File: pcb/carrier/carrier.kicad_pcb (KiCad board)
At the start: 2 copper layers, 152 x 100.2 mm, 42 parts, among them J1 Freeze footswitch, J2 Clear footswitch, J3 In L / Mono, J4 In R (normalled from In L), J5 Out L / Mono, J6 Out R (ring = plug detect), SW1 Single / Multi, SW2 +5 up / down, U1 Daisy Seed

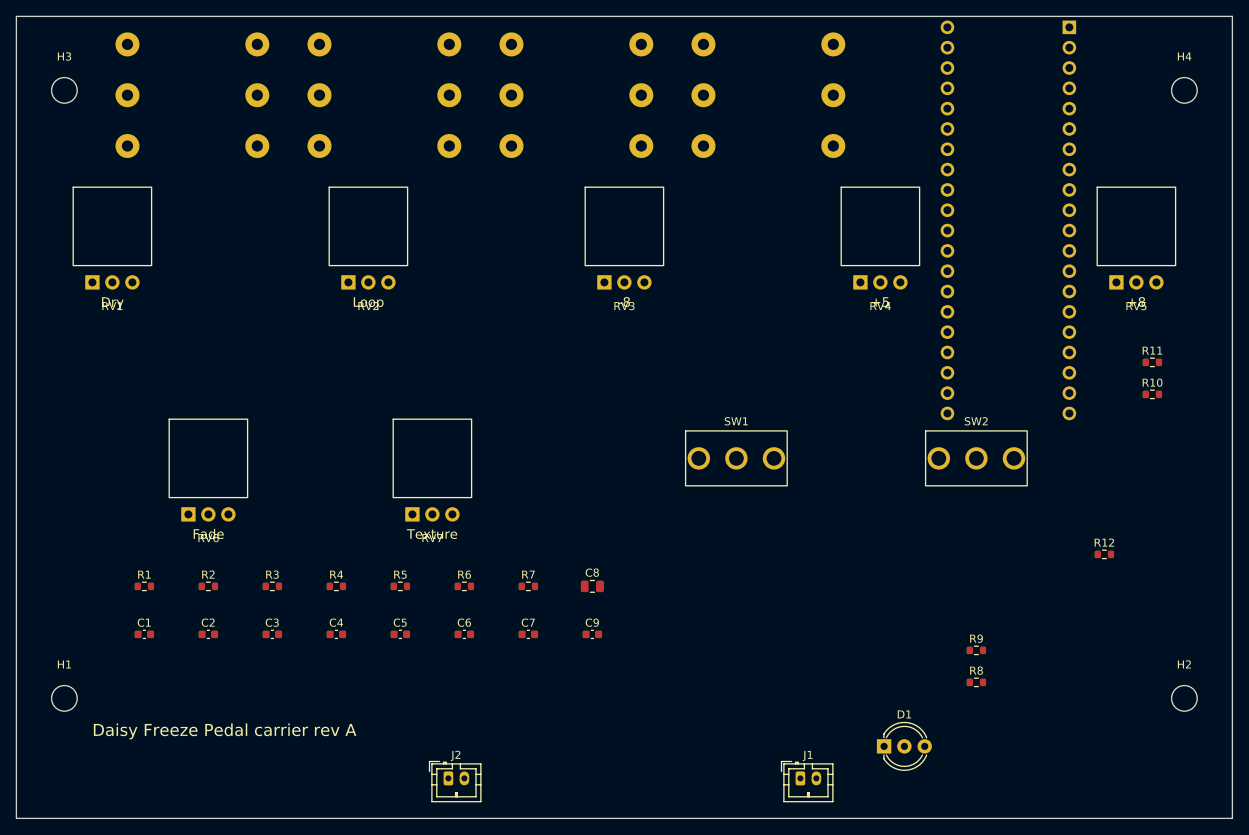
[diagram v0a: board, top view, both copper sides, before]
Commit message: Carrier board: routed, DRC clean, fab outputs
route_pcb.py sets design rules, autoroutes with Freerouting (retrying
until complete), imports the session file, and pours AGND on both
layers; DRC reports 0 violations and 0 unconnected pads. make_fab.py
writes Gerbers, drill files, a zip, and JLC-style BOM and placement
files for the 21 top-side SMD parts.

Pot mounting tabs are now plated (solderable). The jack footprint is a
project copy with its outline on the fab layer, since the jack noses
overhang the rear edge by design.

Co-Authored-By: Claude Opus 5.5 <noreply@anthropic.com>
Claude-Session: https://claude.ai/code/session_01JAavHVgiwWaG4iqEz4KA1Q
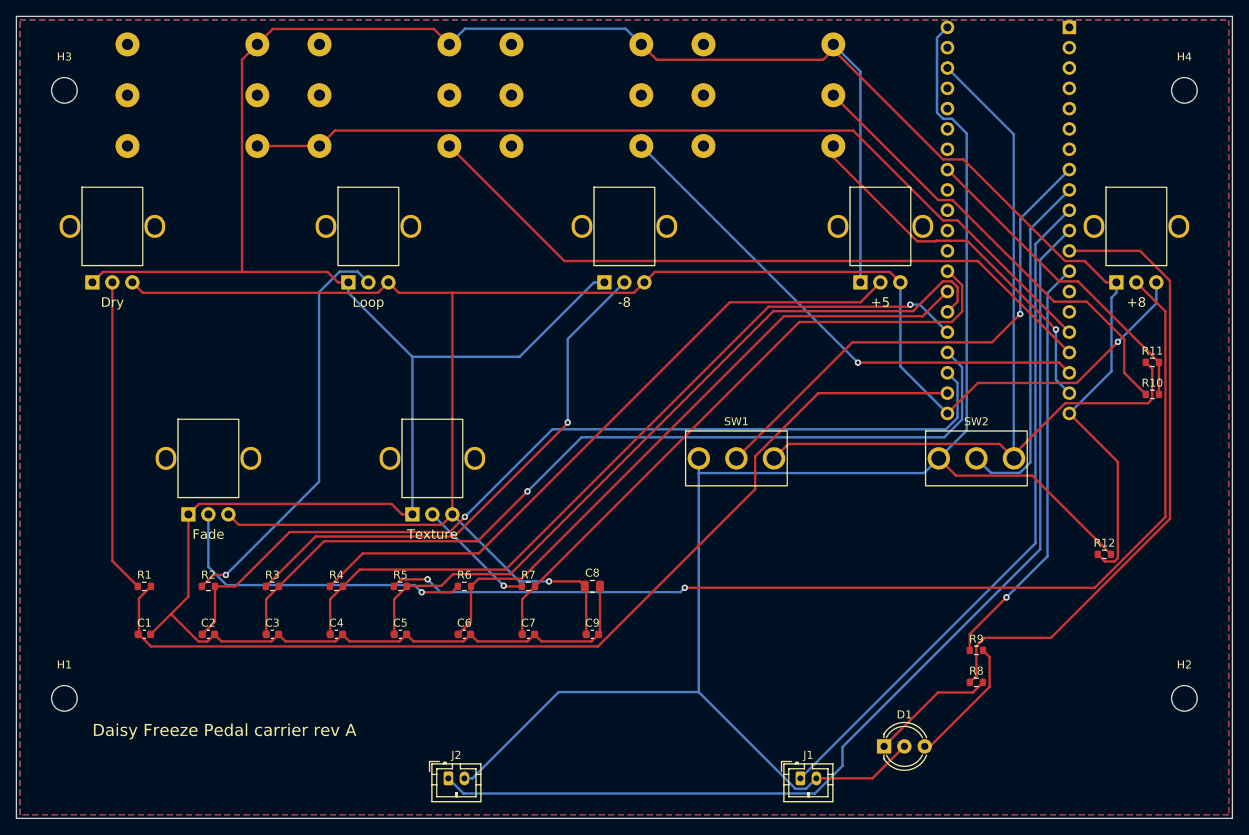
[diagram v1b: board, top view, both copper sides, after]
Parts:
- J3, J4, J5, J6: footprint Connector_Audio:Jack_6.35mm_Neutrik_NMJ6HCD2_Horizontal -> carrier:Jack_6.35mm_Neutrik_NMJ6HCD2_Horizontal_FabOnlySilk
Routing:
- net AGND: track 0.00 -> 432.5 mm
- net +3V3A: track 0.00 -> 235.6 mm, vias 0 -> 2
- net DGND: track 0.00 -> 211.2 mm
- net POT_OCT: track 0.00 -> 132.2 mm, vias 0 -> 2
- net FS_CLEAR: track 0.00 -> 130.1 mm
- net ADC_DRY: track 0.00 -> 123.9 mm
- net ADC_LOOP: track 0.00 -> 114.4 mm, vias 0 -> 1
- net IN_L: track 0.00 -> 112.7 mm
- net ADC_SUB: track 0.00 -> 109.8 mm, vias 0 -> 1
- net +3V3D: track 0.00 -> 109.2 mm
- net ADC_FIFTH: track 0.00 -> 98.2 mm, vias 0 -> 1
- net ADC_OCT: track 0.00 -> 95.2 mm
- net IN_R: track 0.00 -> 88.2 mm
- net FS_FREEZE: track 0.00 -> 84.9 mm
- net POT_FIFTH: track 0.00 -> 84.6 mm
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- added copper zone on B.Cu, net AGND
- added copper zone on F.Cu, net AGND

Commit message: Carrier: single ground pour, verified parts
AGND and DGND now tie to one carrier ground (R12 removed), poured on both
layers and stitched with a via grid; re-routed, DRC 0 violations and 0
unconnected. SMD parts carry manufacturer part numbers checked against
their JLC part pages. README records the jack panel-thickness check
(NMJ6HCD2 is rated under 4.7 mm) and the placement-rotation note.

Co-Authored-By: Claude Opus 5.5 <noreply@anthropic.com>
Claude-Session: https://claude.ai/code/session_01JAavHVgiwWaG4iqEz4KA1Q
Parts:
- removed R12: 0R, Resistor_SMD:R_0603_1608Metric
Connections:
- C1 pad 2: AGND -> GND
- C2 pad 2: AGND -> GND
- C3 pad 2: AGND -> GND
- C4 pad 2: AGND -> GND
- C5 pad 2: AGND -> GND
- C6 pad 2: AGND -> GND
- C7 pad 2: AGND -> GND
- C8 pad 2: AGND -> GND
- C9 pad 2: AGND -> GND
- D1 pad 2: DGND -> GND
- J1 pad 2: DGND -> GND
- J2 pad 2: DGND -> GND
- J3 pad S: AGND -> GND
- J4 pad S: AGND -> GND
- J5 pad S: AGND -> GND
- J6 pad S: AGND -> GND
- RV1 pad 1: AGND -> GND
- RV2 pad 1: AGND -> GND
- RV3 pad 1: AGND -> GND
- RV4 pad 1: AGND -> GND
- RV5 pad 1: AGND -> GND
- RV6 pad 1: AGND -> GND
- RV7 pad 1: AGND -> GND
- SW1 pad 1: DGND -> GND
- SW2 pad 1: DGND -> GND
- U1 pad 20: AGND -> GND
- U1 pad 40: DGND -> GND
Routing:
- net GND: track 0.00 -> 486.0 mm, vias 0 -> 138
- net AGND: track 432.5 -> 0.00 mm
- net DGND: track 211.2 -> 0.00 mm
- net LED_RED_DRV: track 79.5 -> 59.1 mm, vias 0 -> 1
- net OUT_R: track 46.9 -> 61.3 mm, vias 1 -> 0
- net ADC_FADE: track 81.5 -> 94.1 mm, vias 0 -> 1
- net POT_OCT: track 132.2 -> 119.8 mm, vias 2 -> 1
- net ADC_OCT: track 95.2 -> 103.9 mm
- net POT_DRY: track 39.3 -> 46.4 mm
- net POT_SUB: track 66.7 -> 60.6 mm, vias 1 -> 0
- net TGL_FIFTH_DIR: track 44.1 -> 38.4 mm
- net ADC_TEX: track 80.1 -> 85.3 mm, vias 0 -> 1
- net TGL_LAYERS: track 63.6 -> 68.5 mm, vias 1 -> 0
- net ADC_LOOP: track 114.4 -> 119.0 mm
- net POT_FADE: track 39.4 -> 34.9 mm
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- added copper zone on B.Cu, net GND
- added copper zone on F.Cu, net GND
- removed copper zone on B.Cu, net AGND
- removed copper zone on F.Cu, net AGND

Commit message: Apply design review fixes (Seed3 target)
Mechanical (from datasheets):
- Jack axis is 7.53 mm off the PCB (NMJ6HCD2: 15.67 body, axis 8.14
  below its top), not 9.1; back-wall slots moved.
- Toggle bushing base is 10.39 mm above the PCB (E-Switch catalog p.2
  body 8.89 + 1.5 mm M2 pin standoff), so the carrier now hangs 10.39 mm
  under the panel; pots move to 25 mm shafts (11.1 mm above the panel),
  toggles get 5.4 mm of thread for the nut.
- Seed3 geometry: 18 mm wide, 2.5 mm header spacer, USB-C axis 14.2 mm
  below the carrier; USB slot widened to 14 x 9 mm.
- LED sits on a 5 mm spacer to reach its panel hole.

Electrical:
- Out R plug detect now uses the ring-normal contact with the ring
  grounded, so TS and TRS plugs are both detected.
- In L's tip-normal grounds the input when nothing is plugged in.
- 10 uF series + 100 k bleed on each output, per the Seed3 reference.
- Input pad footprints per channel, fitted as no pad (0R, shunt DNP).

Re-routed: DRC 0 violations, 0 unconnected. BOM excludes DNP parts.

Co-Authored-By: Claude Opus 5.5 <noreply@anthropic.com>
Claude-Session: https://claude.ai/code/session_01JAavHVgiwWaG4iqEz4KA1Q
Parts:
- added C10: 10u, Capacitor_SMD:C_0805_2012Metric, F.Cu at (90.0, 144.0)
- added C11: 10u, Capacitor_SMD:C_0805_2012Metric, F.Cu at (122.0, 144.0)
- added R13: 100k, Resistor_SMD:R_0603_1608Metric, F.Cu at (90.0, 148.0)
- added R14: 100k, Resistor_SMD:R_0603_1608Metric, F.Cu at (122.0, 148.0)
- added R15: 0R, Resistor_SMD:R_0603_1608Metric, F.Cu at (44.0, 144.0)
- added R16: DNP 10k, Resistor_SMD:R_0603_1608Metric, F.Cu at (44.0, 148.0)
- added R17: 0R, Resistor_SMD:R_0603_1608Metric, F.Cu at (66.0, 144.0)
- added R18: DNP 10k, Resistor_SMD:R_0603_1608Metric, F.Cu at (66.0, 148.0)
- J3: value In L / Mono -> In L / Mono (grounded when empty)
- J6: value Out R (ring = plug detect) -> Out R (ring switch = plug detect)
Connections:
- J3 pad T: IN_L -> JIN_L
- J3 pad TN: unconnected-(J3-PadTN) -> GND
- J4 pad T: IN_R -> JIN_R
- J4 pad TN: IN_L -> JIN_L
- J5 pad T: OUT_L -> JOUT_L
- J6 pad R: OUTR_RING -> GND
- J6 pad RN: unconnected-(J6-PadRN) -> OUTR_SENSE
- J6 pad T: OUT_R -> JOUT_R
- R10 pad 1: OUTR_RING -> OUTR_SENSE
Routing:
- net GND: track 486.0 -> 589.9 mm, vias 138 -> 113
- net OUTR_SENSE: track 0.00 -> 83.0 mm
- net OUTR_RING: track 56.2 -> 0.00 mm
- net JIN_L: track 0.00 -> 37.3 mm
- net JOUT_L: track 0.00 -> 34.4 mm, vias 0 -> 1
- net JOUT_R: track 0.00 -> 31.8 mm, vias 0 -> 1
- net JIN_R: track 0.00 -> 30.4 mm, vias 0 -> 1
- net OUT_L: track 65.2 -> 93.0 mm, vias 0 -> 2
- net IN_R: track 89.8 -> 111.7 mm
- net OUT_R: track 61.3 -> 43.7 mm
- net IN_L: track 113.2 -> 125.7 mm
- net FS_CLEAR: track 134.1 -> 121.6 mm
- net POT_OCT: track 119.8 -> 131.7 mm, vias 1 -> 0
- net +3V3A: track 237.4 -> 248.1 mm, vias 1 -> 0
- net ADC_OCT: track 103.9 -> 94.6 mm
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
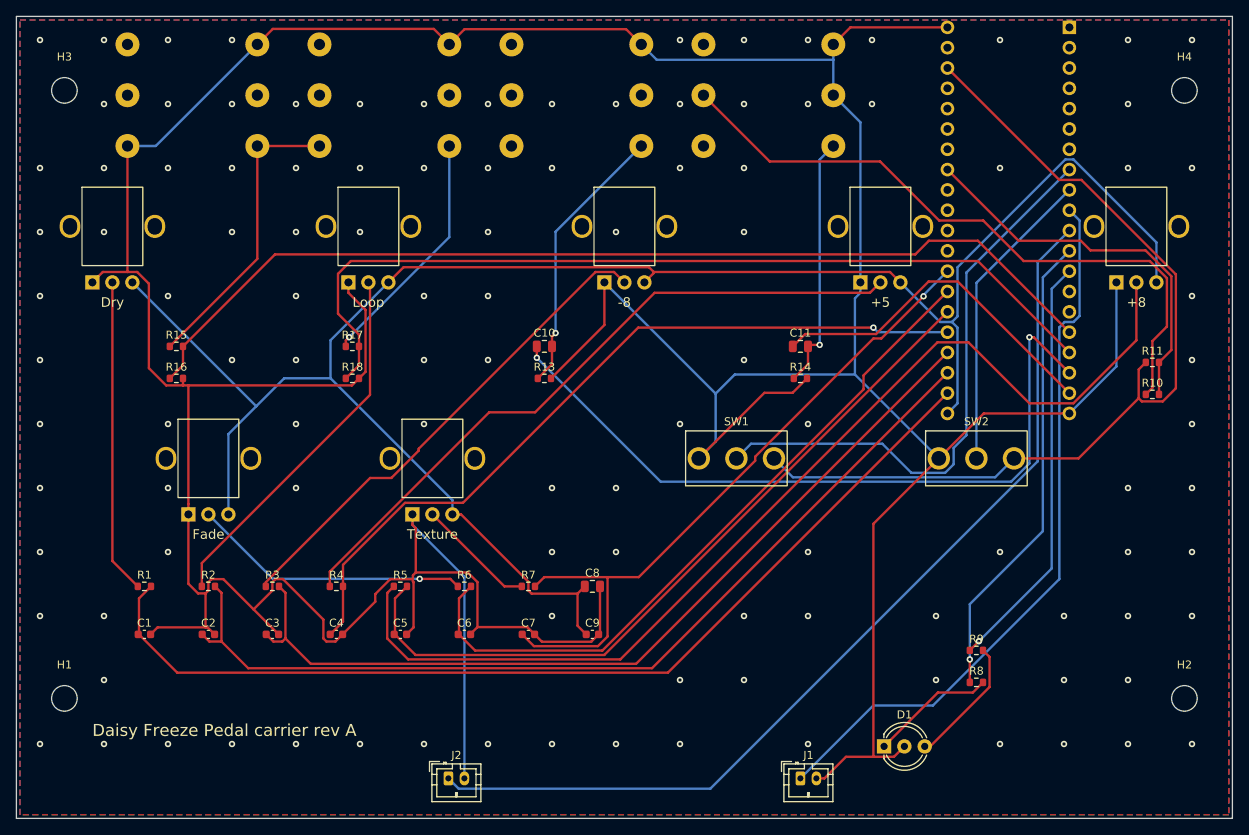
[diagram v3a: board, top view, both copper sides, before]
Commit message: Rev B carrier: bare board, all through-hole, mono in / stereo out
Drops fab assembly. The board is all through-hole with six small parts:
two output coupling caps, two bleed resistors, two LED resistors. Pot
RC filters, supply caps, input pads, the In R jack and the plug-detect
resistors are gone (pots straight to the ADCs, Out R detect and switches
on internal pull-ups). Mono input feeds both codec inputs; stereo out
kept. Three jacks on the back wall. Re-routed, DRC 0 violations.
make_fab.py now writes Gerbers plus a hand-solder bom.csv.

Co-Authored-By: Claude Opus 5.5 <noreply@anthropic.com>
Claude-Session: https://claude.ai/code/session_01JAavHVgiwWaG4iqEz4KA1Q
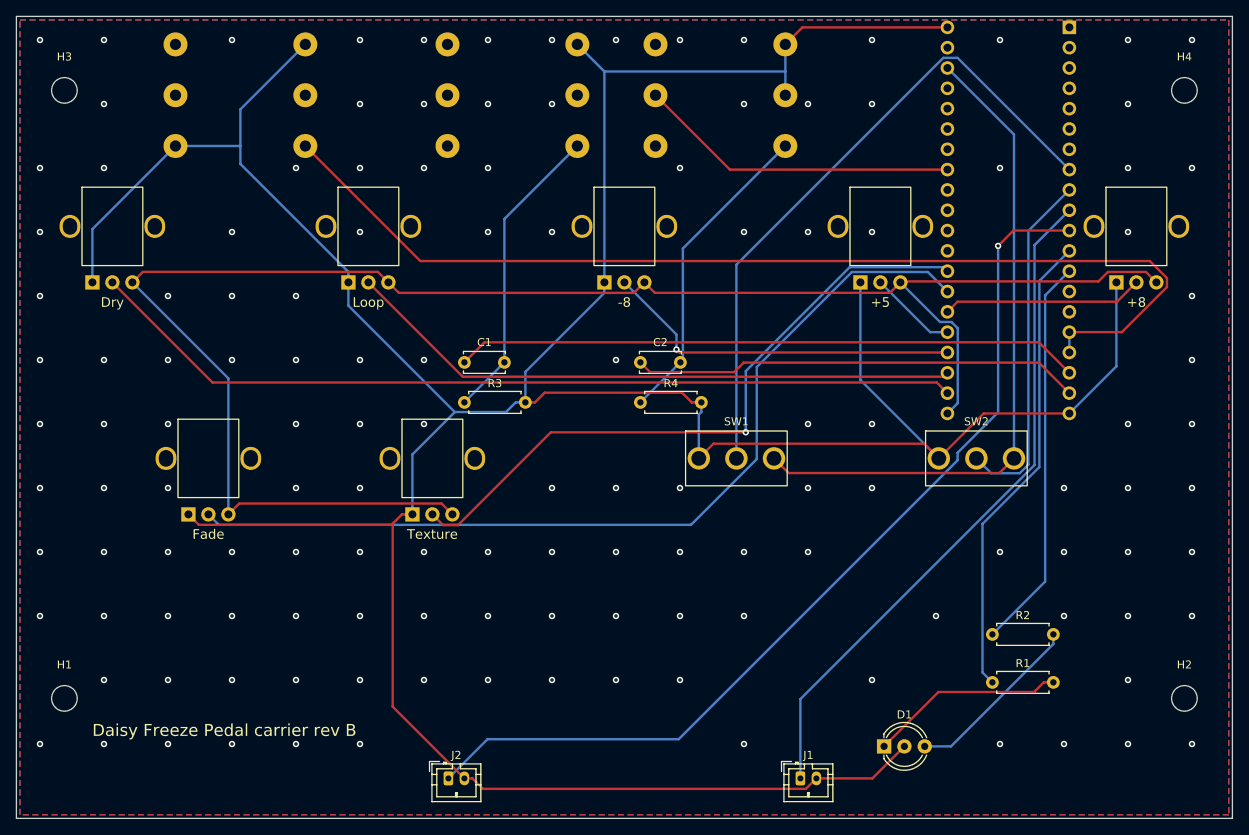
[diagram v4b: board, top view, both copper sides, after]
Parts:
- removed C10, C11, C8: 10u, Capacitor_SMD:C_0805_2012Metric
- removed C3, C4, C5, C6, C7, C9: 100n, Capacitor_SMD:C_0603_1608Metric
- removed J6: Out R (ring switch = plug detect), carrier:Jack_6.35mm_Neutrik_NMJ6HCD2_Horizontal_FabOnlySilk
- removed R10, R5, R6, R7: 1k, Resistor_SMD:R_0603_1608Metric
- removed R11, R13, R14: 100k, Resistor_SMD:R_0603_1608Metric
- removed R15, R17: 0R, Resistor_SMD:R_0603_1608Metric
- removed R16, R18: DNP 10k, Resistor_SMD:R_0603_1608Metric
- removed R8, R9: 470, Resistor_SMD:R_0603_1608Metric
- C1, C2: value 100n -> 10u; footprint Capacitor_SMD:C_0603_1608Metric -> Capacitor_THT:C_Disc_D5.0mm_W2.5mm_P5.00mm
- J3: value In L / Mono (grounded when empty) -> In (mono; grounded when empty)
- J4: value In R (normalled from In L) -> Out L / Mono
- J5: value Out L / Mono -> Out R (ring switch = plug detect)
- R1, R2: value 1k -> 470; footprint Resistor_SMD:R_0603_1608Metric -> Resistor_THT:R_Axial_DIN0207_L6.3mm_D2.5mm_P7.62mm_Horizontal
- R3, R4: value 1k -> 100k; footprint Resistor_SMD:R_0603_1608Metric -> Resistor_THT:R_Axial_DIN0207_L6.3mm_D2.5mm_P7.62mm_Horizontal
- U1: value Daisy Seed -> Daisy Seed3
- moved R1 106.7 mm to (146.0, 186.0)
- moved R2 98.2 mm to (146.0, 180.0)
- moved C2 63.8 mm to (102.0, 146.0)
- moved C1 52.5 mm to (80.0, 146.0)
- moved R4 44.4 mm to (102.0, 151.0)
- moved R3 33.2 mm to (80.0, 151.0)
- moved J5 18.0 mm to (120.1, 119.0)
- moved J4 16.0 mm to (94.1, 119.0)
- moved J3 6.00 mm to (60.1, 119.0)
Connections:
- C1 pad 1: ADC_DRY -> OUT_L
- C1 pad 2: GND -> JOUT_L
- C2 pad 1: ADC_LOOP -> OUT_R
- C2 pad 2: GND -> JOUT_R
- J3 pad T: JIN_L -> AUDIO_IN
- J4 pad T: JIN_R -> JOUT_L
- J4 pad TN: JIN_L -> unconnected-(J4-PadTN)
- J5 pad R: unconnected-(J5-PadR) -> GND
- J5 pad RN: unconnected-(J5-PadRN) -> OUTR_DETECT
- J5 pad T: JOUT_L -> JOUT_R
- R1 pad 1: POT_DRY -> LED_RED_DRV
- R1 pad 2: ADC_DRY -> LED_RED
- R2 pad 1: POT_LOOP -> LED_GRN_DRV
- R2 pad 2: ADC_LOOP -> LED_GRN
- R3 pad 1: POT_SUB -> JOUT_L
- R3 pad 2: ADC_SUB -> GND
- R4 pad 1: POT_FIFTH -> JOUT_R
- R4 pad 2: ADC_FIFTH -> GND
- U1 pad 16: IN_L -> AUDIO_IN
- U1 pad 17: IN_R -> AUDIO_IN
- U1 pad 22: ADC_DRY -> POT_DRY
- U1 pad 23: ADC_LOOP -> POT_LOOP
- U1 pad 24: ADC_SUB -> POT_SUB
- U1 pad 25: ADC_FIFTH -> POT_FIFTH
- U1 pad 26: ADC_OCT -> POT_OCT
- U1 pad 27: ADC_FADE -> POT_FADE
- U1 pad 28: ADC_TEX -> POT_TEX
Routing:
- net AUDIO_IN: track 0.00 -> 132.7 mm
- net GND: track 589.9 -> 462.0 mm, vias 113 -> 135
- net IN_L: track 125.7 -> 0.00 mm
- net ADC_DRY: track 124.2 -> 0.00 mm
- net ADC_LOOP: track 117.4 -> 0.00 mm
- net IN_R: track 111.7 -> 0.00 mm
- net ADC_SUB: track 110.0 -> 0.00 mm
- net POT_OCT: track 131.7 -> 25.1 mm
- net ADC_FIFTH: track 97.4 -> 0.00 mm, vias 1 -> 0
- net ADC_OCT: track 94.6 -> 0.00 mm
- net ADC_FADE: track 88.2 -> 0.00 mm
- net ADC_TEX: track 87.5 -> 0.00 mm, vias 1 -> 0
- net OUTR_SENSE: track 83.0 -> 0.00 mm
- net POT_FADE: track 34.9 -> 113.8 mm, vias 1 -> 0
- net POT_FIFTH: track 85.6 -> 11.0 mm
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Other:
- board text added: "Daisy Freeze Pedal carrier rev B"
- board text removed: "Daisy Freeze Pedal carrier rev A"
